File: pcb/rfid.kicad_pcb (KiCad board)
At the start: 2 copper layers, 24 parts, among them IC1 ATMEGA8-P, P1 CONN_2, P2 CONN_4, Q1 BS107, Q2 BC547, U1 LM358, X1 8MHz

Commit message: starting new pcb routing
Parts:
- removed D1: 1N4148, D3
- removed P1: CONN_2, SIL-2
- removed P2: CONN_4, SIL-4
- removed Q1: BS107, TO92
- removed Q2: BC547, TO92
- removed U1: LM358, DIP-8__300
- removed X1: 8MHz, HC-18UV
- added C10: 100n, c_0805, B.Cu at (132.1, 101.6)
- added C11: 1u, c_0805, B.Cu at (141.0, 101.6)
- added C12: 1n, c_0805, B.Cu at (143.0, 101.6)
- added C13: 100n, c_0805, B.Cu at (131.6, 111.0)
- added C14: 4.7u, c_tant_B, B.Cu at (128.8, 127.3)
- added C15: 100n, c_0805, B.Cu at (131.6, 107.2)
- added C16: 1n, c_0805, B.Cu at (140.2, 90.7)
- added C17: 100u, c_tant_D, B.Cu at (189.0, 88.6)
- added C18: 100u, c_tant_D, B.Cu at (189.0, 93.7)
- added C19: 100u, c_tant_D, B.Cu at (187.7, 84.8)
- added C20: 100n, c_0805, B.Cu at (136.1, 88.6)
- added C21: 1n, c_0805, B.Cu at (136.1, 90.7)
- added C22: 100n, c_0805, B.Cu at (140.2, 88.6)
- added C6: DV1, c_0805, B.Cu at (140.2, 82.5)
- added C7: DV2, c_0805, B.Cu at (140.2, 86.6)
- added C8: 100n, c_0805, B.Cu at (145.8, 97.8)
- added C9: 100n, c_0805, B.Cu at (130.0, 101.6)
- added D3: LED_R, LED-0805, B.Cu at (128.3, 117.3)
- added D4: LED_G, LED-0805, B.Cu at (128.0, 106.2)
- added D5: LED_PD, LED-0805, B.Cu at (150.1, 130.3)
- added D6: LED_PA, LED-0805, B.Cu at (186.7, 142.2)
- added IC2: ATTINY13A-SS, SO8N, B.Cu at (135.3, 108.8)
- added J1: USB, PIN_ARRAY_4x1, F.Cu at (135.6, 128.5)
- added L3: 22uH 3A, R3-LARGE_PADS, F.Cu at (138.7, 95.2)
- added R11: 68, SM0805, B.Cu at (191.8, 144.8)
- added R12: 100, SM0805, B.Cu at (120.7, 106.2)
- added R13: 100, SM0805, B.Cu at (124.2, 106.2)
- added R14: 100, SM0805, B.Cu at (149.1, 126.2)
- added R15: 100, SM0805, B.Cu at (152.9, 126.2)
- added R16: 100, SM0805, B.Cu at (157.0, 126.0)
- added R17: 100, SM0805, B.Cu at (191.8, 142.2)
- added R18: 100, SM0805, B.Cu at (179.1, 142.2)
- added R19: 100, SM0805, B.Cu at (182.9, 142.2)
- added SP1: SPEAKER, BUZ3-5, F.Cu at (121.9, 96.5)
- C1: value 1n5 -> RES; footprint C2 -> c_0805; moved to B.Cu
- C2: value 4n7 -> DV1; footprint C2 -> c_0805; moved to B.Cu
- C3: value 15n -> RES; footprint C2 -> c_0805; moved to B.Cu
- C4: value 22p -> DV1; footprint C2 -> c_0805; moved to B.Cu
- C5: value 22p -> RES; footprint C2 -> c_0805; moved to B.Cu
- IC1: value ATMEGA8-P -> EM4095; footprint DIP-28__300 -> SO16E; moved to B.Cu
- R1: value 100 -> 10; footprint R3 -> SM1210L; moved to B.Cu
- R10: value 100K -> 1k; footprint R3 -> SM0805; moved to B.Cu
- R2: value 1K -> 2K2; footprint R3 -> SM0805; moved to B.Cu
- R3: value 270K -> 68; footprint R3 -> SM0805; moved to B.Cu
- R4: value 4K7 -> 68; footprint R3 -> SM0805; moved to B.Cu
- R5: value 1K8 -> 0; footprint R3 -> SM0805; moved to B.Cu
- R6, R9: value 33K -> 0; footprint R3 -> SM0805; moved to B.Cu
- R7: value 390K -> 0; footprint R3 -> SM0805; moved to B.Cu
- R8: value 1K2 -> 0; footprint R3 -> SM0805; moved to B.Cu
- moved R8 128.6 mm to (195.6, 143.5), turned to 0 degrees
- moved R9 104.1 mm to (199.4, 143.5), turned to 0 degrees
- moved R3 80.0 mm to (136.4, 114.8), turned to 270 degrees
- moved C2 73.7 mm to (140.2, 84.6), turned to 180 degrees
- moved C3 66.0 mm to (136.1, 82.5), turned to 180 degrees
- moved R6 64.0 mm to (134.1, 101.6)
- moved R7 59.0 mm to (136.1, 101.6), turned to 90 degrees
- moved R2 54.5 mm to (132.8, 126.0)
- moved C1 52.5 mm to (136.1, 84.6), turned to 180 degrees
- moved R1 49.1 mm to (145.5, 90.7), turned to 90 degrees
- moved L1 47.9 mm to (131.1, 88.9), turned to 270 degrees
- moved R10 45.3 mm to (138.9, 106.9)
- moved R5 39.4 mm to (138.9, 101.6), turned to 90 degrees
- moved C4 39.1 mm to (140.2, 80.5), turned to 180 degrees
- moved R4 38.8 mm to (134.1, 114.8), turned to 270 degrees
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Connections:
- C1 pad 1: N-0000037 -> N-0000034
- C1 pad 2: GND -> N-0000033
- C2 pad 1: N-0000038 -> N-0000033
- C2 pad 2: GND -> N-0000031
- C3 pad 1: N-0000038 -> N-0000034
- C3 pad 2: N-0000032 -> N-0000033
- C4 pad 1: GND -> N-0000033
- C4 pad 2: N-000006 -> N-0000031
- C5 pad 1: GND -> N-0000034
- C5 pad 2: N-000005 -> N-0000033
- IC1 pad 1: (no net) -> GND
- IC1 pad 10: N-000005 -> N-0000015
- IC1 pad 11: (no net) -> N-0000013
- IC1 pad 12: (no net) -> N-0000028
- IC1 pad 13: (no net) -> N-0000012
- IC1 pad 14: N-0000010 -> N-000001
- IC1 pad 15: N-0000013 -> N-0000027
- IC1 pad 16: (no net) -> N-0000026
- IC1 pad 3: (no net) -> N-0000017
- IC1 pad 4: N-000004 -> +5VA
- IC1 pad 5: (no net) -> GND
- IC1 pad 6: (no net) -> N-0000016
- IC1 pad 8: GND -> N-0000031
- IC1 pad 9: N-000006 -> N-0000014
- L1 pad 1: N-0000034 -> N-0000033
- L1 pad 2: N-0000037 -> N-0000017
- R1 pad 1: +5V -> N-0000016
- R10 pad 1: N-000004 -> +5V
- R10 pad 2: N-000002 -> N-000005
- R2 pad 1: N-0000036 -> +5V
- R2 pad 2: N-0000013 -> N-0000030
- R3 pad 1: GND -> N-000003
- R3 pad 2: N-0000038 -> N-0000032
- R4 pad 1: N-000007 -> N-000002
- R4 pad 2: +5V -> N-0000030
- R5 pad 2: N-000007 -> N-0000028
- R6 pad 1: N-0000033 -> GND
- R6 pad 2: N-0000032 -> N-000001
- R7 pad 2: N-0000033 -> N-000001
- R8 pad 1: N-000008 -> N-0000020
- R9 pad 1: N-000002 -> N-0000020
- R9 pad 2: +5V -> GND
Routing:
- net +5V: track 88.3 -> 19.3 mm
- net GND: track 0.00 -> 51.8 mm
- net N-0000011: track 44.5 -> 0.00 mm
- net N-0000012: track 48.5 -> 8.86 mm
- net N-000002: track 34.4 -> 2.05 mm
- net N-000004: track 26.6 -> 0.00 mm
- net N-000007: track 26.4 -> 0.00 mm
- net N-000008: track 25.2 -> 0.00 mm
- net N-0000036: track 15.7 -> 0.00 mm
- net N-0000038: track 13.6 -> 0.00 mm
- net N-0000032: track 13.4 -> 0.00 mm
- net N-0000031: track 0.00 -> 13.3 mm
- net N-000006: track 12.1 -> 0.00 mm
- net N-0000037: track 11.8 -> 0.00 mm
- net N-0000034: track 15.6 -> 4.06 mm
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- removed copper zone on B.Cu, net GND
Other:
- board outline added: 108 x 82.5 mm
- net class Default: clearance 0.254 -> 0.3; trace_width 0.4 -> 0.3; via_dia 0.889 -> 1.6; via_drill 0.635 -> 0.6
- rule trace_clearance: 0.254 -> 0.3
- rule trace_min: 0.254 -> 0.3
- rule via_min_drill: 0.508 -> 0.6
- rule via_min_size: 0.889 -> 1.6
- board text removed: "Aiwaras 2014"

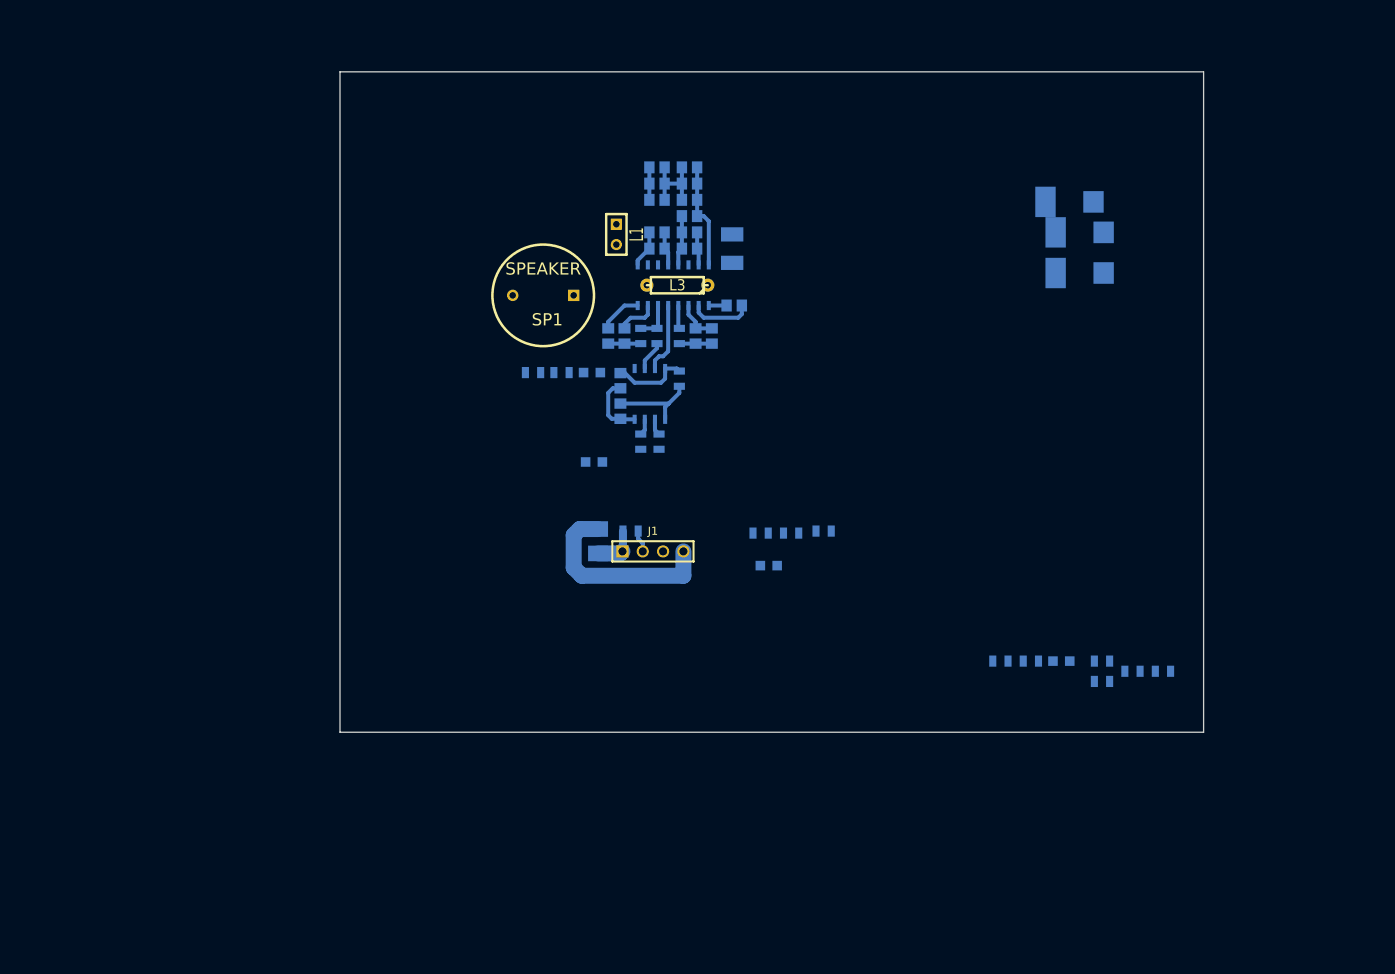
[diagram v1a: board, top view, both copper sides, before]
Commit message: routing pcb with only few GND left unconnected
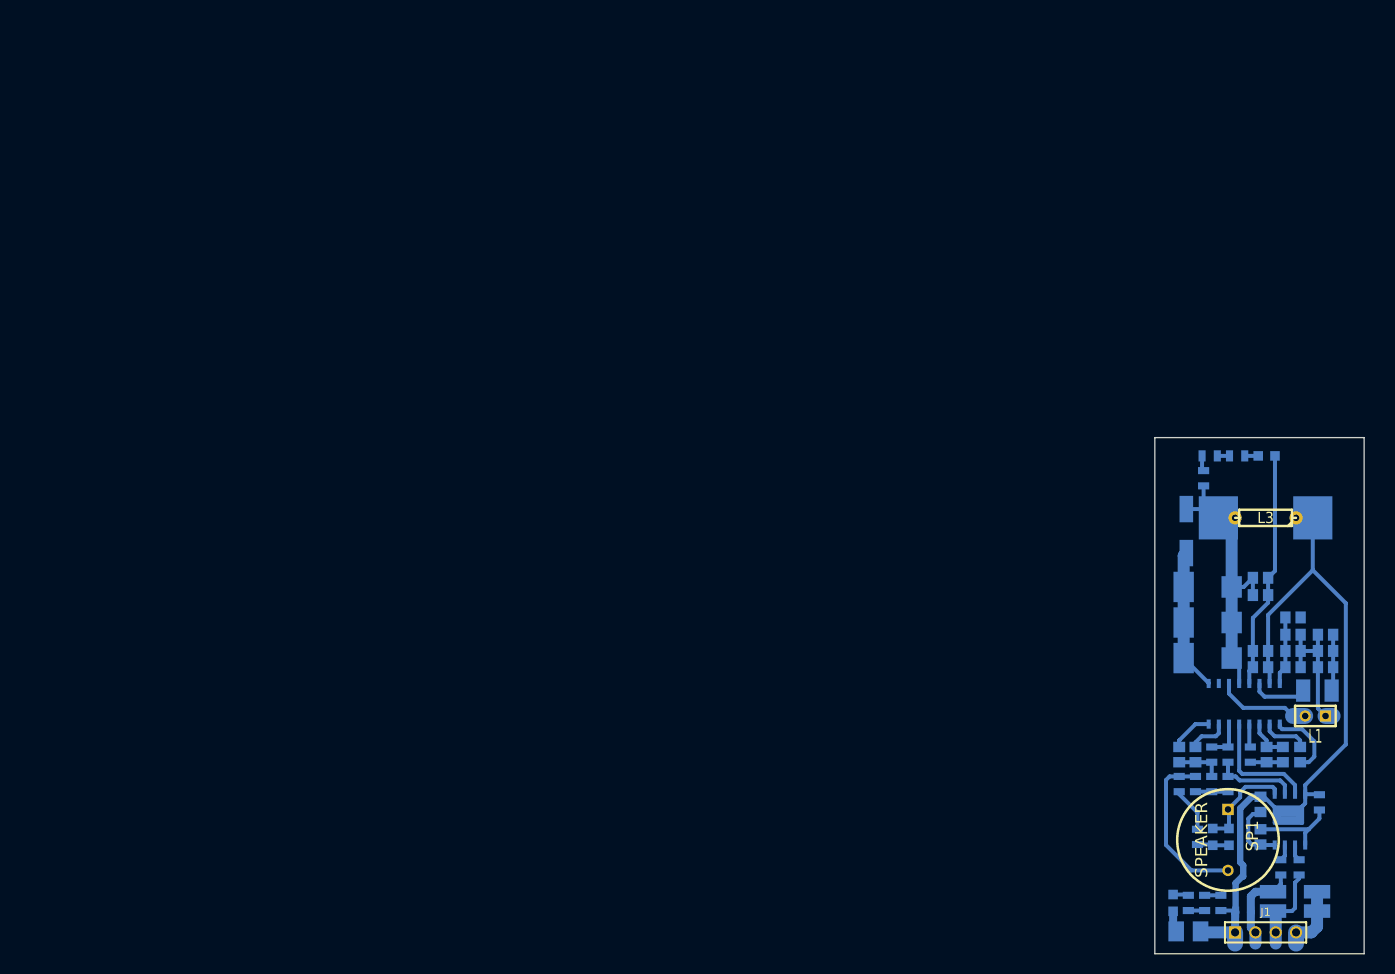
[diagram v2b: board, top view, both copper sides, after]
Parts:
- added D1: 3V6, Diode-MiniMELF_Handsoldering_RevA_27July2010, B.Cu at (215.9, 173.5)
- added D2: 3V6, Diode-MiniMELF_Handsoldering_RevA_27July2010, B.Cu at (215.9, 171.1)
- added D7: 5V6, Diode-MiniMELF_Handsoldering_RevA_27July2010, B.Cu at (202.3, 126.0)
- added L2: 22uH 3A, Choke_SMD_Wuerth-WE-PD-Typ-LS_Handsoldering_RevA_27July2010, B.Cu at (212.2, 124.3)
- moved SP1 109.4 mm to (207.5, 164.6), turned to 270 degrees
- moved L1 106.1 mm to (218.4, 149.1), turned to 180 degrees
- moved C5 104.3 mm to (219.7, 143.0), turned to 0 degrees
- moved C3 102.0 mm to (219.7, 141.0), turned to 0 degrees
- moved C1 99.7 mm to (219.7, 138.9), turned to 0 degrees
- moved D4 98.5 mm to (207.6, 164.2), turned to 270 degrees
- moved R13 98.4 mm to (203.7, 164.2), turned to 270 degrees
- moved R4 96.1 mm to (214.1, 168.0)
- moved C13 96.1 mm to (211.6, 164.2)
- moved IC2 96.1 mm to (215.3, 162.1)
- moved R3 96.1 mm to (216.4, 168.0)
- moved R10 95.9 mm to (218.9, 159.9)
- moved C15 95.9 mm to (211.6, 160.1)
- moved R12 95.8 mm to (201.4, 157.6), turned to 270 degrees
- moved C2 95.4 mm to (215.6, 143.0), turned to 0 degrees
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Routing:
- net +5V: track 19.3 -> 118.1 mm
- net +5VA: track 4.25 -> 38.4 mm
- net GND: track 51.8 -> 76.8 mm
- net N-0000021: track 0.00 -> 21.1 mm
- net N-0000025: track 0.00 -> 12.6 mm
- net N-0000017: track 0.00 -> 12.0 mm
- net N-0000032: track 0.00 -> 11.5 mm
- net N-0000030: track 2.78 -> 11.7 mm
- net N-0000033: track 10.3 -> 17.7 mm
- net N-0000014: track 2.22 -> 9.39 mm
- net N-0000016: track 0.00 -> 7.06 mm
- net N-0000019: track 3.74 -> 10.5 mm
- net N-0000012: track 8.86 -> 14.7 mm
- net N-0000024: track 0.00 -> 5.71 mm
- net N-0000031: track 13.3 -> 8.54 mm
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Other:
- board size 108 x 82.5 mm -> 26.2 x 64.5 mm

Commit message: finalising pcb routing
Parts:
- added P1: CONN_1, smd_pad_2mm, B.Cu at (217.7, 166.6)
- added P2: CONN_1, smd_pad_2mm, B.Cu at (207.8, 166.5)
- added P3: CONN_1, smd_pad_2mm, B.Cu at (215.9, 158.4)
- added P4: CONN_1, smd_pad_2mm, B.Cu at (210.6, 158.4)
- added P5: CONN_1, smd_pad_2mm, B.Cu at (213.2, 158.4)
- added P6: CONN_1, smd_pad_2mm, B.Cu at (218.6, 158.4)
- moved D3 4.21 mm to (203.6, 160.5)
- moved D4 4.21 mm to (205.6, 160.5)
- moved R13 4.21 mm to (201.7, 160.5)
- moved SP1 3.15 mm to (205.1, 162.6), turned to 225 degrees
- moved C8 2.29 mm to (218.7, 153.2), turned to 90 degrees
- moved R4 2.22 mm to (212.1, 168.9), turned to 180 degrees
- moved R10 2.16 mm to (217.6, 161.5)
- moved C15 2.16 mm to (210.2, 161.8)
- moved IC2 2.16 mm to (213.9, 163.7)
- moved C13 2.16 mm to (210.2, 165.9)
- moved R3 1.17 mm to (215.6, 168.9), turned to 0 degrees
- moved C11 0.80 mm to (212.6, 153.2)
- moved C16 0.80 mm to (211.8, 142.2)
- moved C2 0.80 mm to (215.9, 142.2)
- moved C20 0.80 mm to (211.8, 133.2)
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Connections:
- net N-000005 renamed /RST
- D3 pad 2: N-0000025 (its old number) -> /MOSI
- D4 pad 1: N-0000025 (its old number) -> /MOSI
- IC1 pad 13: N-0000012 (its old number) -> /SCK
- IC2 pad 5: N-0000025 (its old number) -> /MOSI
- IC2 pad 6: N-0000019 (its old number) -> /MISO
- IC2 pad 7: N-0000012 (its old number) -> /SCK
- R7 pad 1: N-0000019 (its old number) -> /MISO
- R8 pad 2: N-0000019 (its old number) -> /MISO
- SP1 pad 1: N-0000025 (its old number) -> /MOSI
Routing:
- net GND: track 76.8 -> 102.1 mm, vias 0 -> 5
- net /SCK: track 0.00 -> 17.4 mm
- net N-0000012 (its old number): track 14.7 -> 0.00 mm
- net N-0000025 (its old number): track 12.6 -> 0.00 mm
- net /MISO: track 0.00 -> 11.2 mm
- net /MOSI: track 0.00 -> 10.5 mm
- net N-0000019 (its old number): track 10.5 -> 0.00 mm
- net +5V: track 118.1 -> 126.1 mm
- net N-0000017: track 21.1 -> 13.7 mm
- net N-0000019: track 5.71 -> 1.84 mm
- net N-0000024: track 6.00 -> 9.18 mm
- net N-0000014: track 9.39 -> 6.41 mm
- net /RST: track 10.9 -> 12.9 mm
- net (no net): vias 0 -> 1
- added copper zone on B.Cu, net GND
- added copper zone on F.Cu, net GND
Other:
- board size 26.2 x 64.5 mm -> 27.9 x 66.2 mm
- board text added: "COPYLEFT 2014"
- board text added: "HH USB RFID READER 125KHz"
- board text added: "REV 1.0"

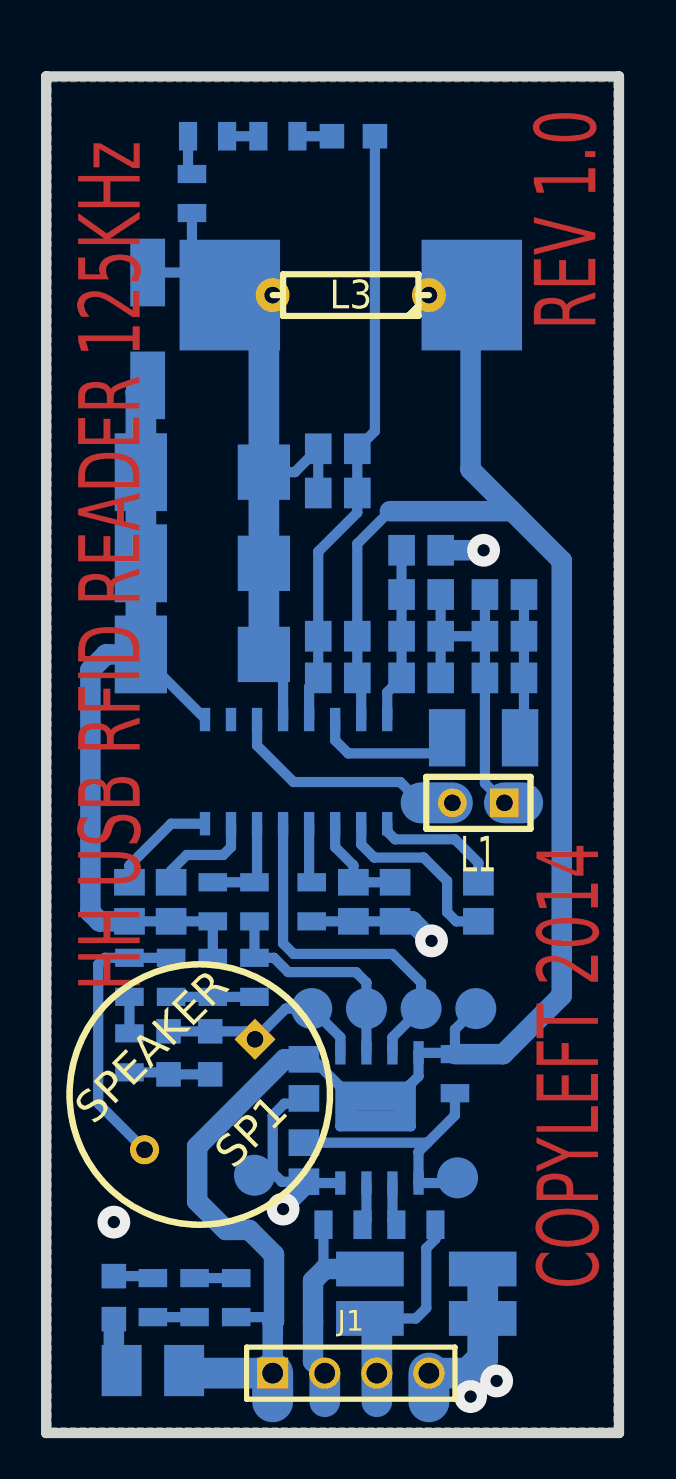
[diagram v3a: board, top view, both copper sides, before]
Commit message: shrinking PCB and adding BOM
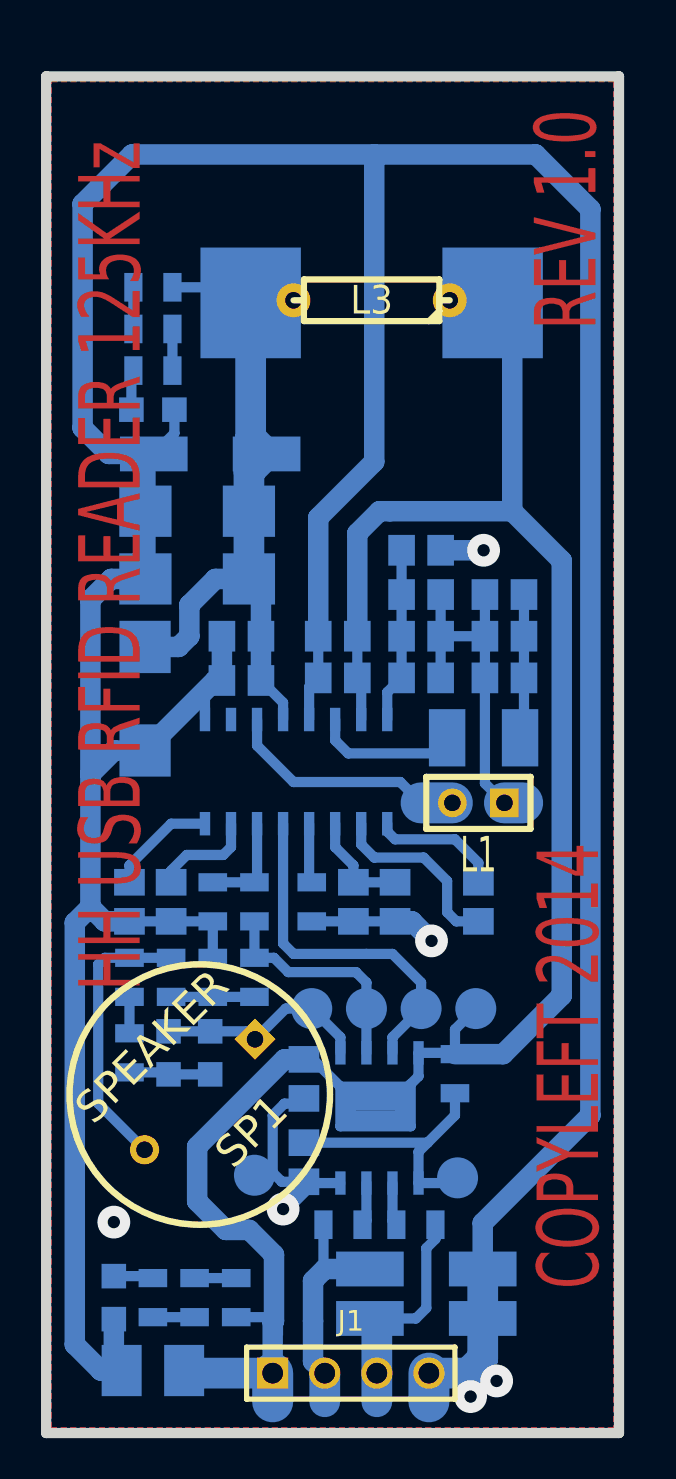
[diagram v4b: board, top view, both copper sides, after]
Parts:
- C17, C18, C19: footprint c_tant_D -> c_tant_C
- moved D6 16.5 mm to (202.8, 129.2)
- moved R19 13.0 mm to (202.8, 127.3), turned to 180 degrees
- moved C21 10.3 mm to (207.1, 140.2), turned to 0 degrees
- moved C20 10.3 mm to (207.1, 142.4), turned to 0 degrees
- moved R18 9.77 mm to (202.8, 125.2)
- moved D7 6.82 mm to (205.6, 131.3), turned to 0 degrees
- moved R17 4.95 mm to (202.8, 123.2), turned to 180 degrees
- moved C18 3.53 mm to (202.4, 143.3), turned to 90 degrees
- moved C17 1.92 mm to (205.0, 134.1)
- moved L2 1.09 mm to (213.5, 124.0)
- moved L3 1.05 mm to (213.5, 123.8)
- moved C19 0.80 mm to (205.0, 137.4)
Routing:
- net GND: track 102.1 -> 228.7 mm
- net +5VA: track 38.4 -> 33.2 mm
- net +5V: track 126.1 -> 123.5 mm
- net N-0000010: track 1.52 -> 2.03 mm
